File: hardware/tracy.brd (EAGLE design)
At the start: 50 x 38 mm, 88 parts, among them IC1 SIM900, J1 U.FL, J2 U.FL, Q1 si2305cd, Q4 si2305cd, T1 BC846, T2 BC846, U1 SPX5205 3v3, U2 3339, U3 TC1014 2V8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

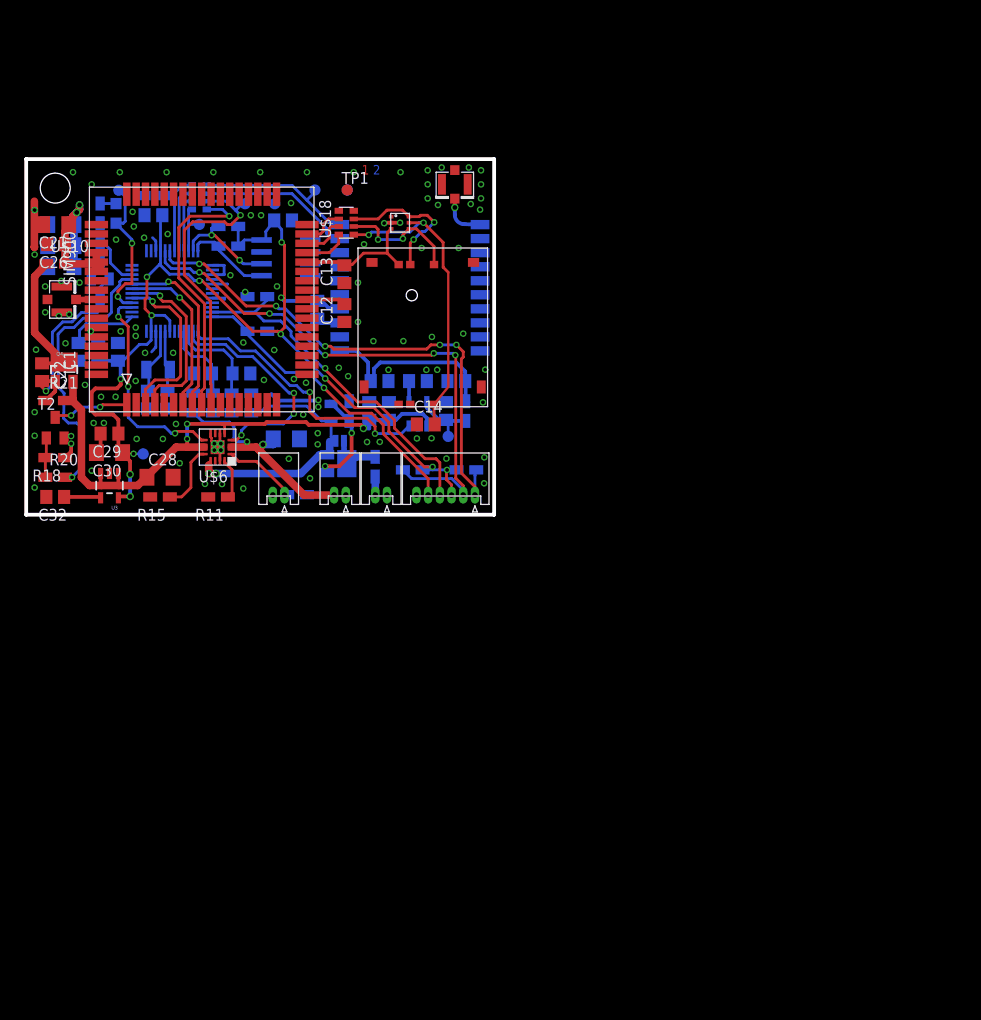
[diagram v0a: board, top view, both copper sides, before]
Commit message: rev3 - initial switch to msp430fr5994
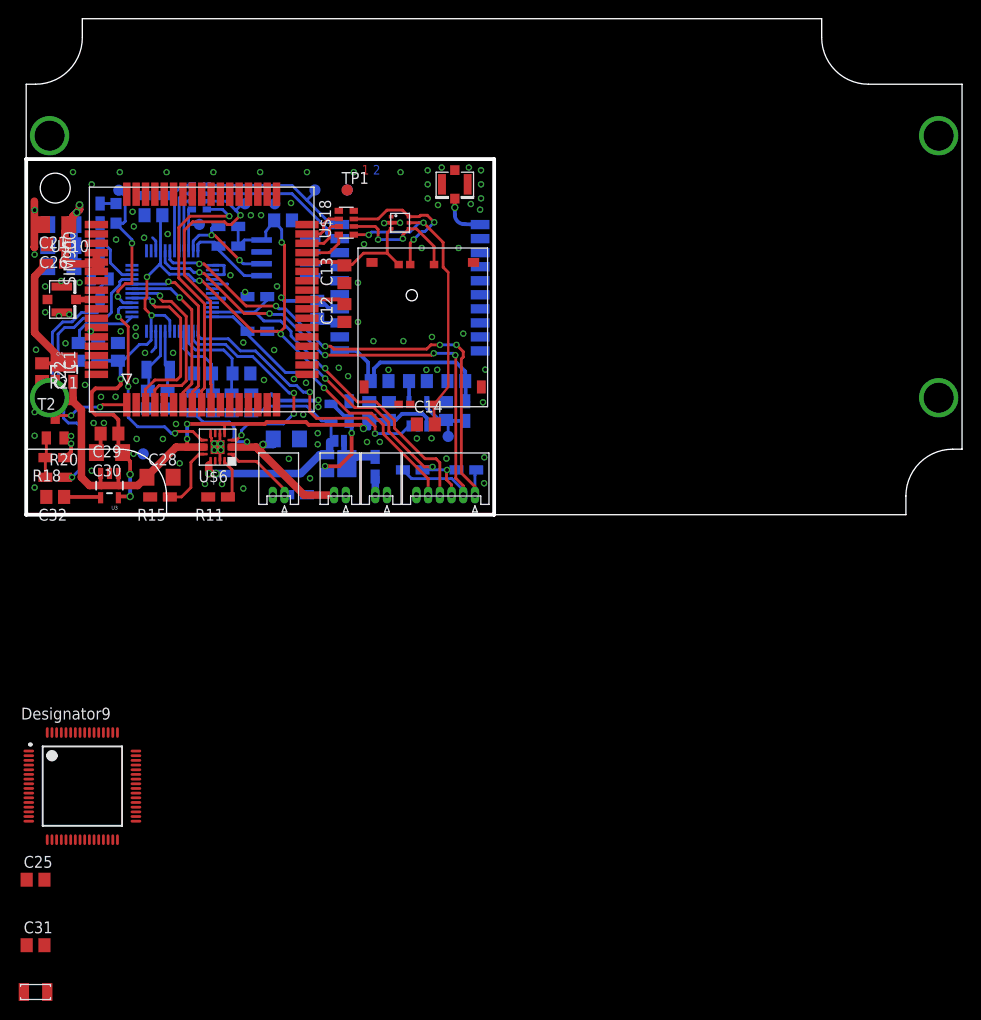
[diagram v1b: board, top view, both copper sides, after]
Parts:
- added C25, C31: 22pF, rcl:C0805
- added U$23: G203C, Simplex-Enclosures:G203C
- added U5: MSP430FR5994, Simplex-ICs:PM0064A_N
- added Y2: 32768Hz CFPX-217 12.5pF, Simplex-FreqCtrl:CRYSTAL-SMD-3.2X1.5
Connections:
- new net !RST: U5.31
- new net N$12: C31.1, U5.62, Y2.P$1
- new net N$13: C25.1, U5.61, Y2.P$2
- new net UCA0RX: U5.33
- new net UCA0TX: U5.32
- new net UCA1RX: U5.29
- new net UCA1TX: U5.28
- new net UCA2RX: U5.54
- new net UCA2TX: U5.53
- new net UCB2SCL: U5.10
- new net UCB2SDA: U5.9
- net 2V8: now also U5.16, U5.49, U5.64
- net GND: now also C25.2, C31.2, U$23.SH@1, U$23.SH@2, U$23.SH@3, U$23.SH@4, U5.15, U5.48, U5.57, U5.60, U5.63
- net TEST: now also U5.30
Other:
- board size 50 x 38 mm -> 100 x 53 mm
